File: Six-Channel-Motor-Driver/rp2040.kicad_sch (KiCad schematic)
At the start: 12 parts

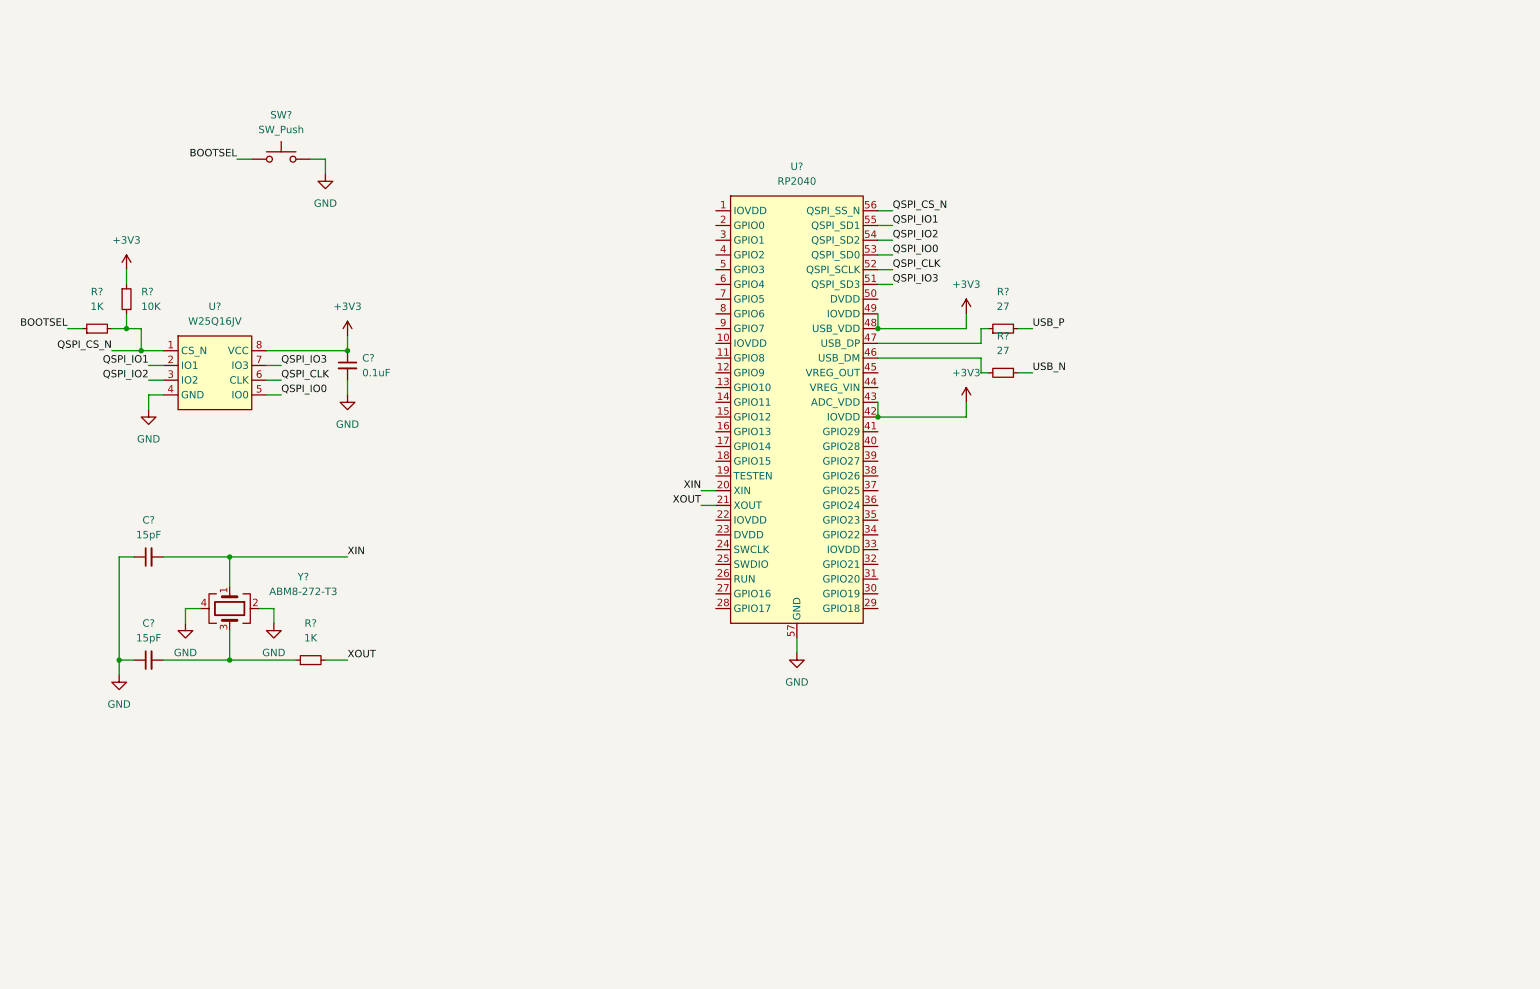
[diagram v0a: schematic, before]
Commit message: More work on MCU schematic
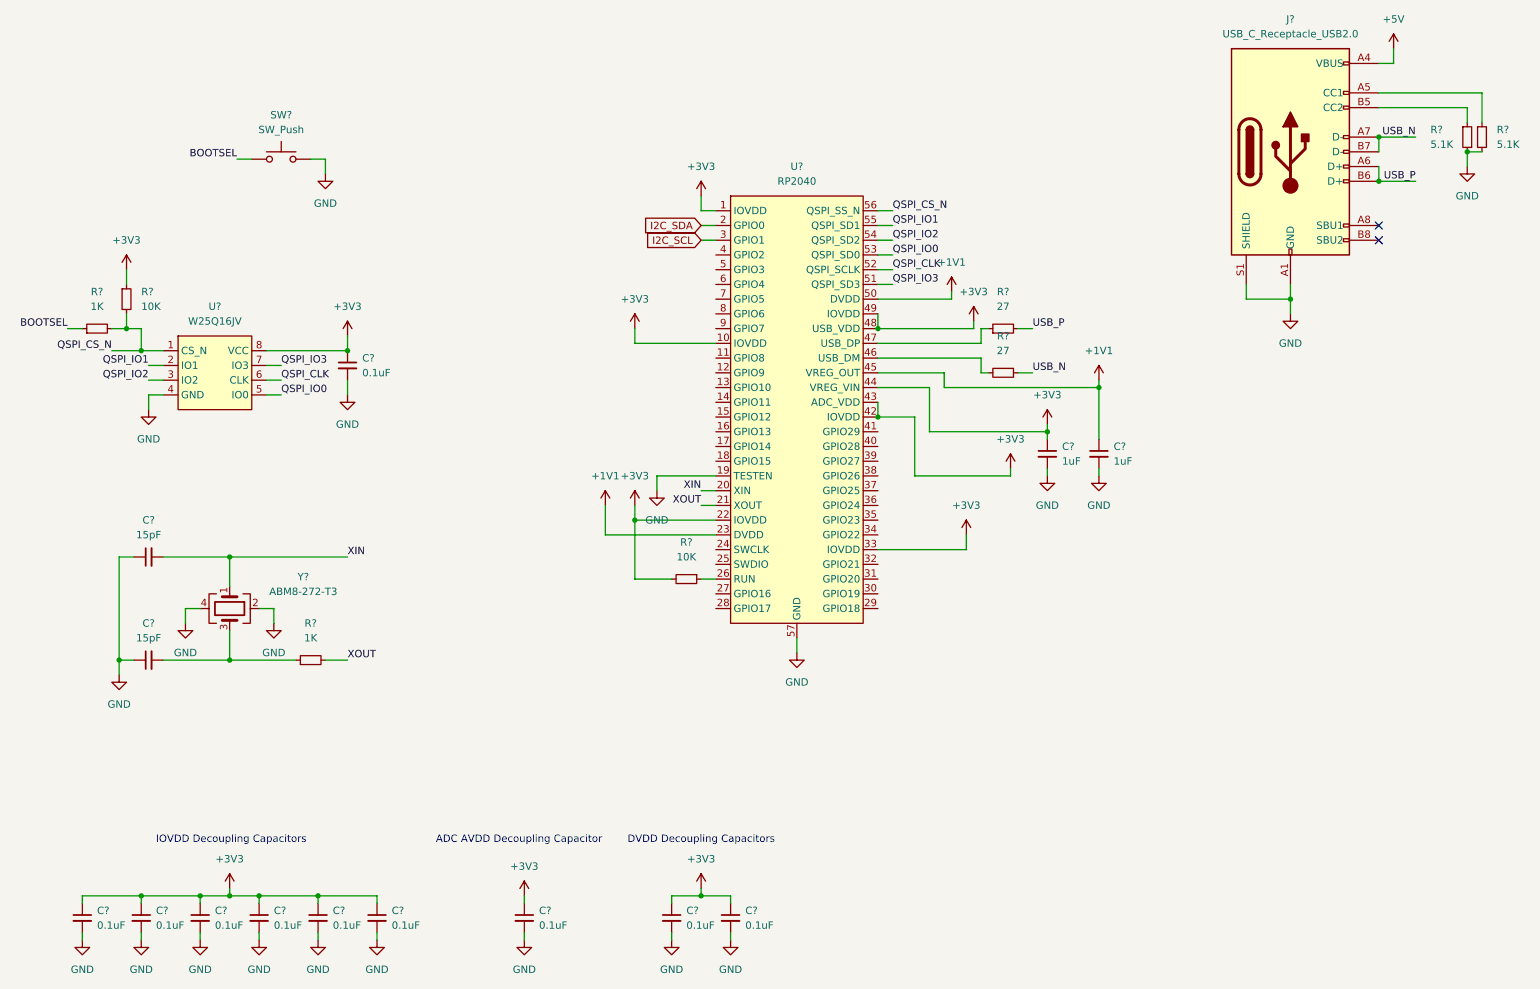
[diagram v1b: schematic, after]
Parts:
- added C? (x9): 0.1uF, symbol Device:C_Small
- added C? (x2): 1uF, symbol Device:C_Small
- added J?: USB_C_Receptacle_USB2.0, symbol Connector:USB_C_Receptacle_USB2.0
- added R? (x2): 5.1K, symbol Device:R_Small
- added R?: 10K, symbol Device:R_Small
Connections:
- net +3V3: now also U?.1 (IOVDD), U?.10 (IOVDD), U?.22 (IOVDD), U?.33 (IOVDD), U?.44 (VREG_VIN), C?.1, C?.1, C?.1, C?.1, C?.1, C?.1, C?.1, C?.1, C?.1, C?.1, R?.2
- net GND: now also U?.19 (TESTEN), C?.2, C?.2, C?.2, C?.2, C?.2, C?.2, C?.2, C?.2, C?.2, C?.2, C?.2, J?.A1 (GND), J?.A12 (GND), J?.B1 (GND), J?.B12 (GND), J?.S1 (SHIELD), R?.2, R?.2
- net USB_N: now also J?.A7 (D-), J?.B7 (D-)
- net USB_P: now also J?.A6 (D+), J?.B6 (D+)
- net I2C_SDA: now reaches U?.2 (GPIO0)
- net +1V1: now reaches U?.23 (DVDD)
- net +1V1: now also U?.45 (VREG_OUT), U?.50 (DVDD), C?.1
- net at U?.26 (RUN): now also R?.1
- net I2C_SCL: now reaches U?.3 (GPIO1)
- new net: J?.A5 (CC1), R?.1
- new net: J?.B5 (CC2), R?.1
- new net +5V: J?.A4 (VBUS), J?.A9 (VBUS), J?.B4 (VBUS), J?.B9 (VBUS)
- no-connect marks 0 -> 2
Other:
- note added: "ADC AVDD Decoupling Capacitor"
- note added: "DVDD Decoupling Capacitors"
- note added: "IOVDD Decoupling Capacitors"

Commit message: Added start of driver blocks
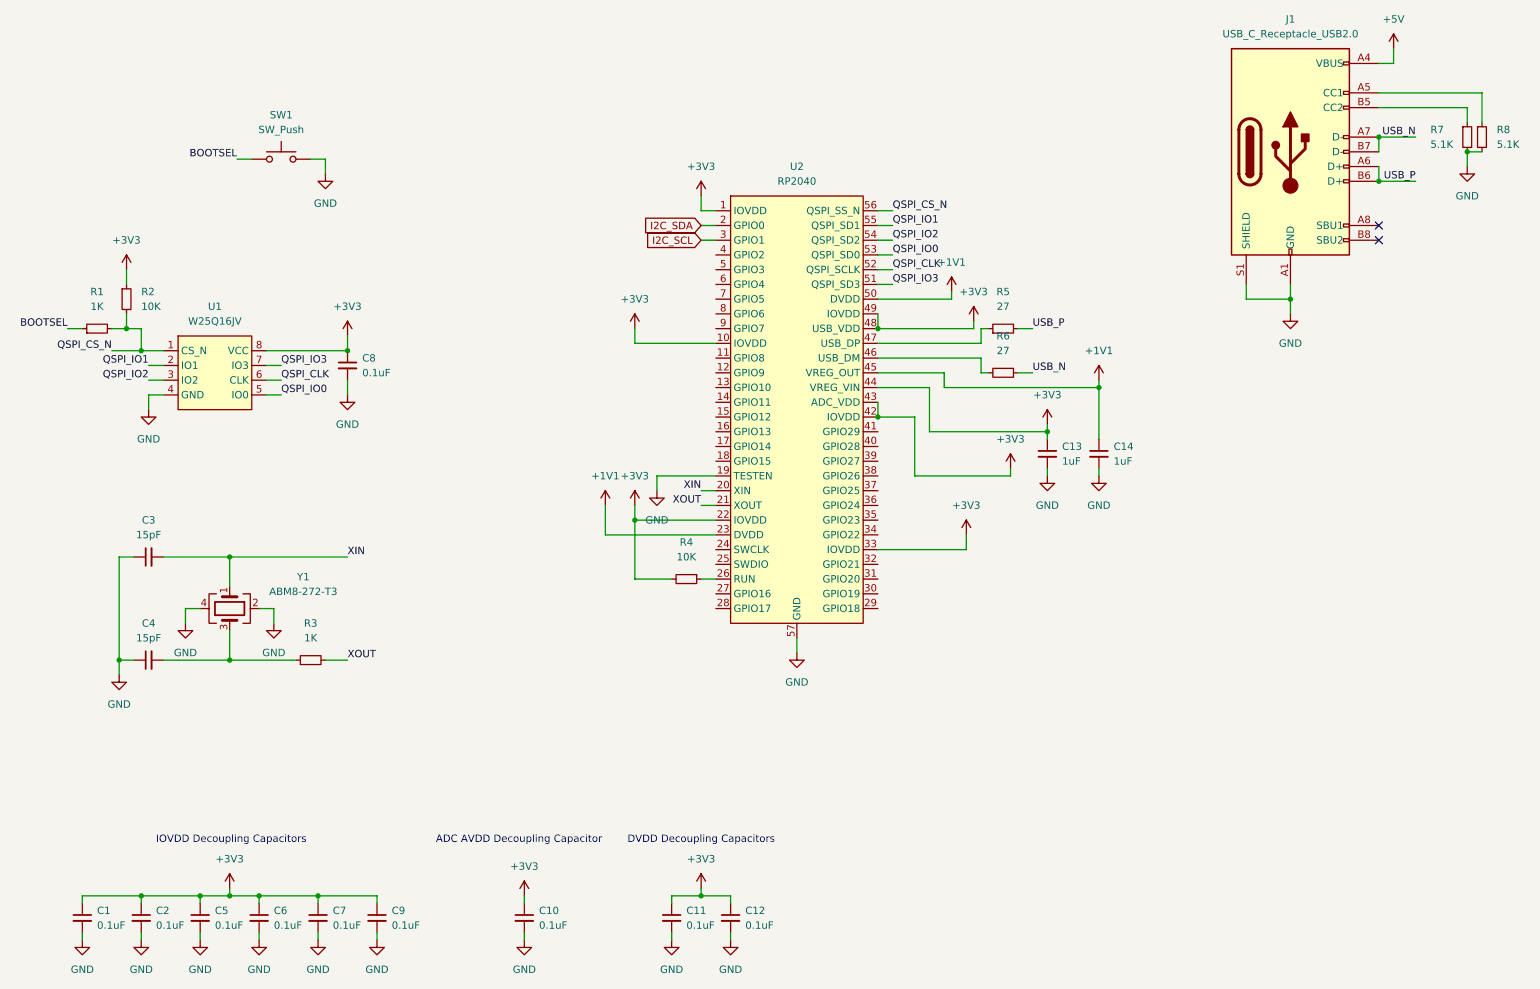
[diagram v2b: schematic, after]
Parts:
- C1, C10, C11, C12, C13, C14, C2, C3, C4, C5, C6, C7, C8, C9: renamed from C?; footprint (none) -> Capacitor_SMD:C_0603_1608Metric
- J1: renamed from J?; footprint (none) -> Connector_USB:USB_C_Receptacle_Molex_105450-0101
- R1, R2, R3, R4, R5, R6, R7, R8: renamed from R?; footprint (none) -> Resistor_SMD:R_0603_1608Metric
- SW1: renamed from SW?; footprint (none) -> Button_Switch_SMD:SW_SPST_FSMSM
- U1: renamed from U?; footprint (none) -> Package_SO:SOIC-8_3.9x4.9mm_P1.27mm
- U2: renamed from U?; footprint (none) -> Package_DFN_QFN:QFN-56-1EP_7x7mm_P0.4mm_EP3.2x3.2mm
- Y1: renamed from Y?; footprint (none) -> Oscillator:Oscillator_SMD_Abracon_ASE-4Pin_3.2x2.5mm
